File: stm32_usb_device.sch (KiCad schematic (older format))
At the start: 43 parts, among them J1 USB_A, J2 Conn_01x05, J3 Conn_01x03, SW1 RST_SW, SW2 USR_SW, U1 HT7533-1, U2 SRV05-4, U3 STM32F103C8T6, Y1 16M

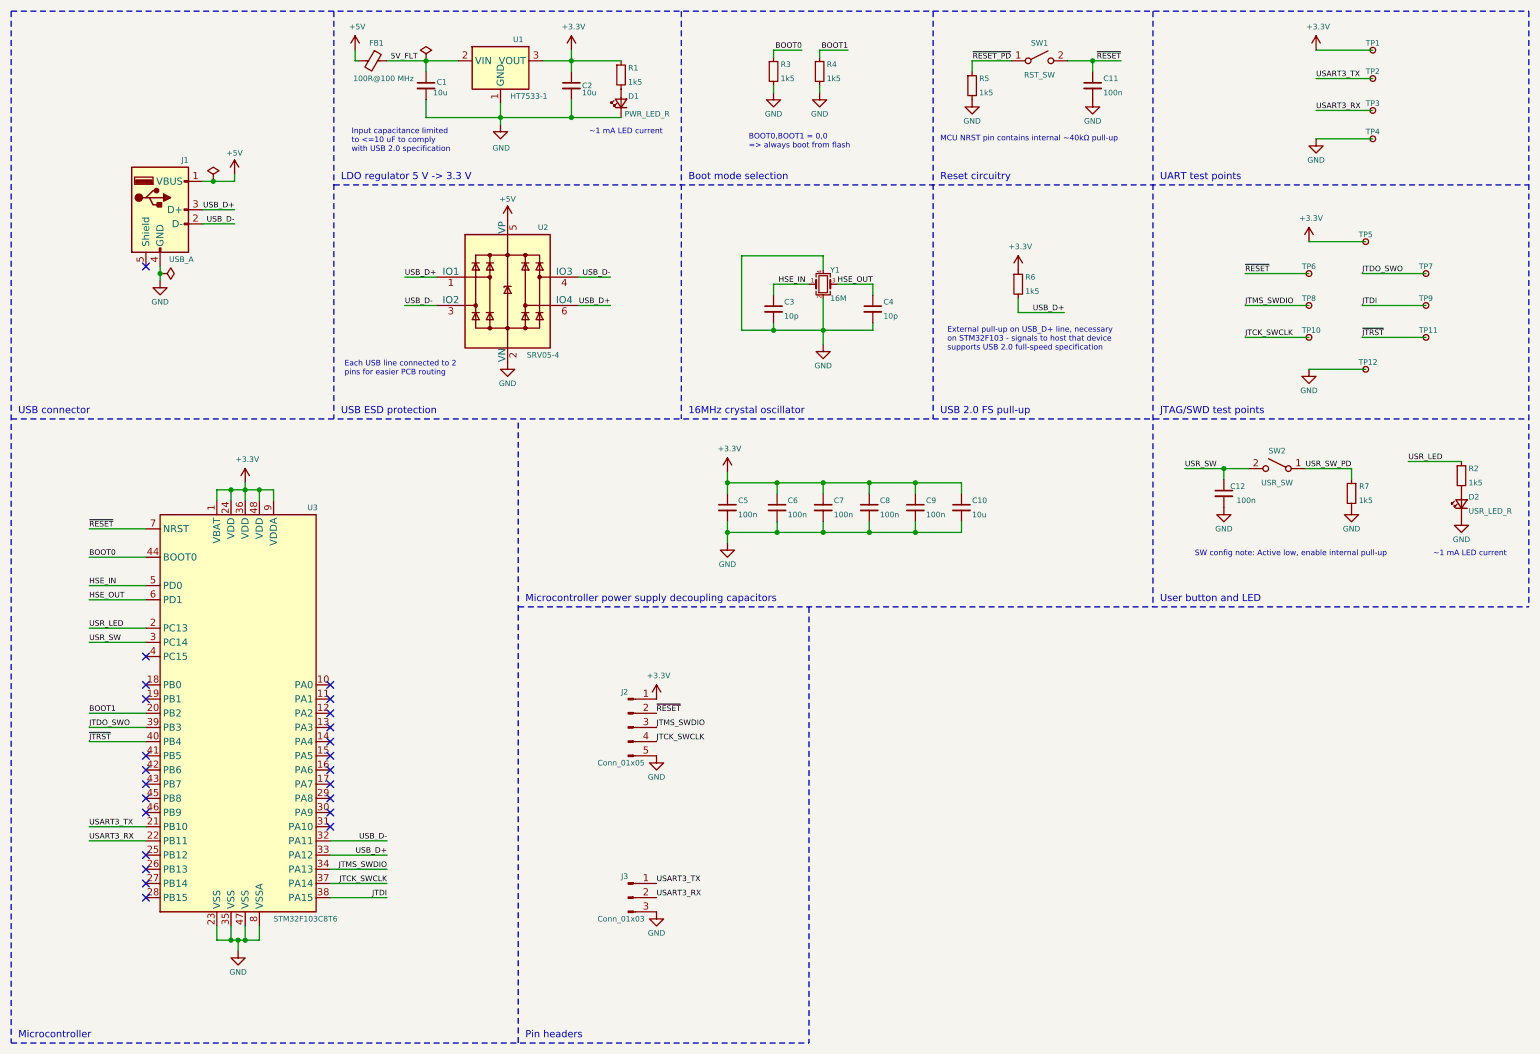
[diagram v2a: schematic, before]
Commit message: Add USB connector and UART isolators
Make initial PCB layout and routing
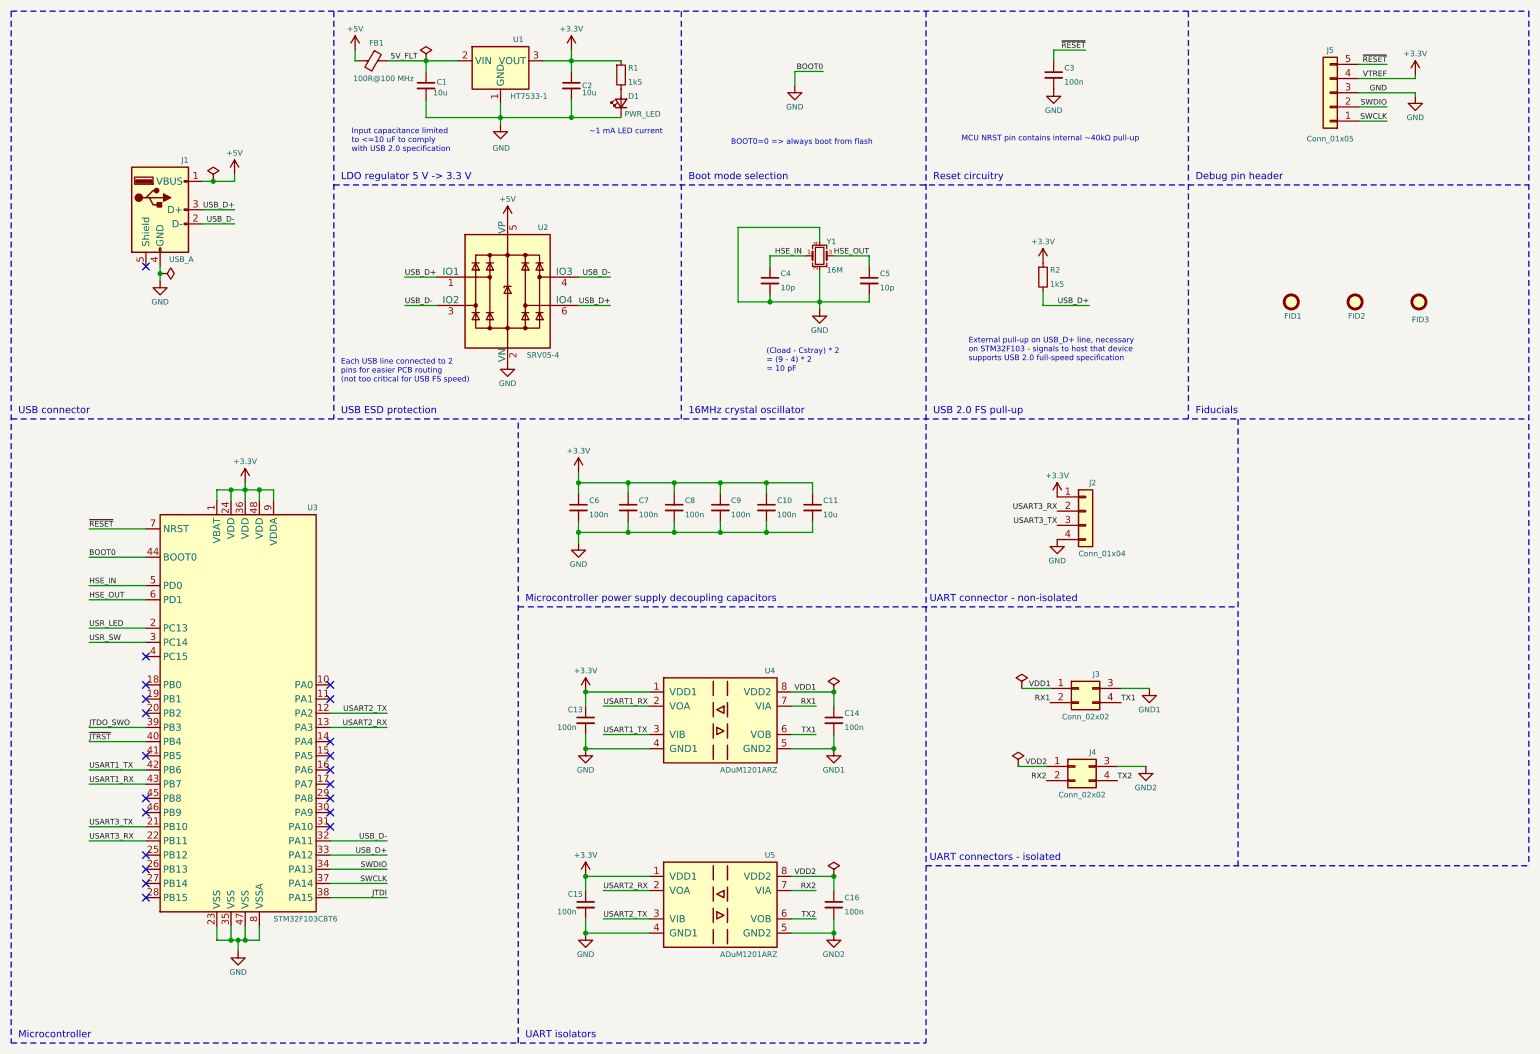
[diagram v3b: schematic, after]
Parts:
- removed C12: 100n, Capacitor_SMD:C_0402_1005Metric, symbol Device:C_Small
- removed D2: USR_LED_R, LED_SMD:LED_0603_1608Metric, symbol Device:LED_Small
- removed J2: Conn_01x05, Connector_PinHeader_2.54mm:PinHeader_1x05_P2.54mm_Vertical, symbol Connector:Conn_01x05_Male
- removed J3: Conn_01x03, Connector_PinHeader_2.54mm:PinHeader_1x03_P2.54mm_Vertical, symbol Connector:Conn_01x03_Male
- removed R2, R3, R4, R5, R7: 1k5, Resistor_SMD:R_0402_1005Metric, symbol Device:R_Small
- removed SW1: RST_SW, Button_Switch_SMD:SW_SPST_CK_RS282G05A3, symbol Switch:SW_SPST
- removed SW2: USR_SW, Button_Switch_SMD:SW_SPST_CK_RS282G05A3, symbol Switch:SW_SPST
- removed TP1, TP10, TP11, TP12, TP2, TP3, TP4, TP5, TP6, TP7, TP8, TP9: TestPoint_Small, TestPoint:TestPoint_Pad_D1.0mm, symbol Connector:TestPoint_Small
- added C13, C14, C15, C16: 100n, Capacitor_SMD:C_0402_1005Metric, symbol Device:C_Small
- added FID1, FID2, FID3: Fiducial, Fiducial:Fiducial_1mm_Mask2mm, symbol Mechanical:Fiducial
- added J2: Conn_01x04, Connector_PinHeader_2.54mm:PinHeader_1x04_P2.54mm_Vertical, symbol Connector_Generic:Conn_01x04
- added J3, J4: Conn_02x02, Connector_PinHeader_2.54mm:PinHeader_2x02_P2.54mm_Horizontal, symbol Connector_Generic:Conn_02x02_Top_Bottom
- added J5: Conn_01x05, Connector_PinHeader_1.27mm:PinHeader_1x05_P1.27mm_Vertical_SMD_Pin1Left, symbol Connector_Generic:Conn_01x05
- added U4, U5: ADuM1201ARZ, Package_SO:SOIC-8_3.9x4.9mm_P1.27mm, symbol Isolator:ADuM1201AR
- D1: value PWR_LED_R -> PWR_LED
- J1: footprint Connector_USB:USB_A_CNCTech_1001-011-01101_Horizontal -> USB_A_connector:USB_A_4pin
- renumbered C9 to C10, C10 to C11, C11 to C3, C3 to C4, C4 to C5, C5 to C6, C6 to C7, C7 to C8, C8 to C9, R6 to R2
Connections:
- net BOOT0 is gone; now on net GND: U3.44 (BOOT0)
- net +3V3: now also C13.1, C15.1, J2.1 (Pin_1), J5.4 (Pin_4), U4.1 (VDD1), U5.1 (VDD1)
- net GND: now also C13.2, C15.2, J2.4 (Pin_4), J5.3 (Pin_3), U4.4 (GND1), U5.4 (GND1)
- net USART3_RX: now also J2.2 (Pin_2)
- net USART3_TX: now also J2.3 (Pin_3)
- net ~RESET: now also J5.5 (Pin_5)
- net USART2_TX: now reaches U3.12 (PA2)
- net USART2_TX: now also U5.3 (VIB)
- net USART2_RX: now reaches U3.13 (PA3)
- net USART2_RX: now also U5.2 (VOA)
- net USART1_TX: now reaches U3.42 (PB6)
- net USART1_TX: now also U4.3 (VIB)
- net USART1_RX: now reaches U3.43 (PB7)
- net USART1_RX: now also U4.2 (VOA)
- net BOOT1: no longer names the net of U3.20 (PB2)
- net JTCK_SWCLK renamed SWCLK
- net SWCLK: now also J5.1 (Pin_1)
- net JTMS_SWDIO renamed SWDIO
- net SWDIO: now also J5.2 (Pin_2)
- new net GND1: C14.2, J3.3 (Pin_3), U4.5 (GND2)
- new net GND2: C16.2, J4.3 (Pin_3), U5.5 (GND2)
- new net RX1: J3.2 (Pin_2), U4.7 (VIA)
- new net RX2: J4.2 (Pin_2), U5.7 (VIA)
- new net TX1: J3.4 (Pin_4), U4.6 (VOB)
- new net TX2: J4.4 (Pin_4), U5.6 (VOB)
- new net VDD1: C14.1, J3.1 (Pin_1), U4.8 (VDD2)
- new net VDD2: C16.1, J4.1 (Pin_1), U5.8 (VDD2)
- no-connect marks 24 -> 21
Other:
- note added: "(Cload - Cstray) * 2\n= (9 - 4) * 2\n= 10 pF"
- note added: "BOOT0=0 => always boot from flash"
- note added: "Debug pin header"
- note added: "Each USB line connected to 2\npins for easier PCB routing\n(not too critical for USB FS speed)"
- note added: "Fiducials"
- note added: "UART connector - non-isolated"
- note added: "UART connectors - isolated"
- note added: "UART isolators"
- note removed: "BOOT0,BOOT1 = 0,0\n=> always boot from flash"
- note removed: "Each USB line connected to 2\npins for easier PCB routing"
- note removed: "JTAG/SWD test points"
- note removed: "Pin headers"
- note removed: "SW config note: Active low, enable internal pull-up"
- note removed: "UART test points"
- note removed: "User button and LED"
- moved on the sheet: C10, C11, C3, C4, C5, C6, C7, C8, C9, R2, Y1

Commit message: Finish PCB routing
Signed-off-by: Tomislav Milkovic <tomislav.milkovic95@gmail.com>
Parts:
- removed C13, C14, C15, C16: 100n, Capacitor_SMD:C_0402_1005Metric, symbol Device:C_Small
- removed J3, J4: Conn_02x02, Connector_PinHeader_2.54mm:PinHeader_2x02_P2.54mm_Horizontal, symbol Connector_Generic:Conn_02x02_Top_Bottom
- removed U4, U5: ADuM1201ARZ, Package_SO:SOIC-8_3.9x4.9mm_P1.27mm, symbol Isolator:ADuM1201AR
- added J1, J2: Conn_01x04, Connector_PinHeader_2.54mm:PinHeader_1x04_P2.54mm_Vertical, symbol Connector_Generic:Conn_01x04
- added R3, R4, R5, R6, R7, R8: 510R, Resistor_SMD:R_0402_1005Metric, symbol Device:R_Small
- C1, C11, C2: JLCPCB Part # (none) -> C96446
- C10, C3, C6, C7, C8, C9: JLCPCB Part # (none) -> C307331
- C4, C5: JLCPCB Part # (none) -> C32949
- FB1: JLCPCB Part # (none) -> C1015
- R1, R2: JLCPCB Part # (none) -> C25867
- U1: JLCPCB Part # (none) -> C14289
- U2: JLCPCB Part # (none) -> C7420376
- U3: JLCPCB Part # (none) -> C8734
- Y1: JLCPCB Part # (none) -> C13738
- renumbered J2 to J3, J1 to J4
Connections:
- net +3V3: now also J1.1 (Pin_1), J2.1 (Pin_1)
- net GND: now also J1.4 (Pin_4), J2.4 (Pin_4)
- net USART1_RX: now also R7.1
- net USART1_TX: now also R8.2
- net USART2_RX: now also R3.1
- net USART2_TX: now also R4.2
- net USART3_RX: now also R5.1; no longer J3.2 (Pin_2)
- net USART3_TX: now also R6.2; no longer J3.3 (Pin_3)
- new net: J1.2 (Pin_2), R7.2
- new net: J1.3 (Pin_3), R8.1
- new net: J2.2 (Pin_2), R3.2
- new net: J2.3 (Pin_3), R4.1
- new net: J3.2 (Pin_2), R5.2
- new net: J3.3 (Pin_3), R6.1
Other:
- note added: "MCU power supply decoupling capacitors"
- note added: "UART connectors"
- note removed: "Microcontroller power supply decoupling capacitors"
- note removed: "UART connector - non-isolated"
- note removed: "UART connectors - isolated"
- note removed: "UART isolators"
- moved on the sheet: J3

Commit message: Remove unused net labels
Signed-off-by: Tomislav Milkovic <tomislav.milkovic95@gmail.com>
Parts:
- C1, C11, C2: JLCPCB Part # C96446 -> (none); LCSC (none) -> C96446
- C10, C3, C6, C7, C8, C9: JLCPCB Part # C307331 -> (none); LCSC (none) -> C307331
- C4, C5: JLCPCB Part # C32949 -> (none); LCSC (none) -> C32949
- D1: LCSC (none) -> C2286
- FB1: JLCPCB Part # C1015 -> (none); LCSC (none) -> C1015
- R1, R2: JLCPCB Part # C25867 -> (none); LCSC (none) -> C25867
- R3, R4, R5, R6, R7, R8: JLCPCB Part # C25123 -> (none); LCSC (none) -> C25123
- U1: JLCPCB Part # C14289 -> (none); LCSC (none) -> C14289
- U2: JLCPCB Part # C7420376 -> (none); LCSC (none) -> C7420376
- U3: JLCPCB Part # C8734 -> (none); LCSC (none) -> C8734
- Y1: JLCPCB Part # C13738 -> (none); LCSC (none) -> C13738
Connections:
- net JTDI: no longer names the net of U3.38 (PA15)
- net JTDO_SWO: no longer names the net of U3.39 (PB3)
- net USR_LED: no longer names the net of U3.2 (PC13)
- net USR_SW: no longer names the net of U3.3 (PC14)
- net ~JTRST: no longer names the net of U3.40 (PB4)
- no-connect marks 21 -> 26
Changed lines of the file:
@@
 F 2 "Package_QFP:LQFP-48_7x7mm_P0.5mm" H 1550 4050 50  0001 R CNN
 F 3 "http://www.st.com/st-web-ui/static/active/en/resource/technical/document/datasheet/CD00161566.pdf" H 2150 5450 50  0001 C CNN
-F 4 "C8734" H 2150 5450 50  0001 C CNN "JLCPCB Part #"
+F 4 "C8734" H 2150 5450 50  0001 C CNN "LCSC"
 	1    2150 5450
 	1    0    0    -1
@@
 F 2 "Package_TO_SOT_SMD:SOT-89-3" H 3950 1275 50  0001 C CIN
 F 3 "https://www.holtek.com/documents/10179/116711/HT75xx-1v250.pdf" H 3950 1050 50  0001 C CNN
-F 4 "C14289" H 3950 950 50  0001 C CNN "JLCPCB Part #"
+F 4 "C14289" H 3950 950 50  0001 C CNN "LCSC"
 	1    3950 950
 	1    0    0    -1
@@
 F 2 "Package_TO_SOT_SMD:SOT-23-6" H 4700 2025 50  0001 C CNN
 F 3 "http://www.onsemi.com/pub/Collateral/SRV05-4-D.PDF" H 4000 2475 50  0001 C CNN
-F 4 "C7420376" H 4000 2475 50  0001 C CNN "JLCPCB Part #"
+F 4 "C7420376" H 4000 2475 50  0001 C CNN "LCSC"
 	1    4000 2475
 	1    0    0    -1
@@
 F 2 "Capacitor_SMD:C_0603_1608Metric" H 3425 1025 50  0001 C CNN
 F 3 "~" H 3425 1025 50  0001 C CNN
-F 4 "C96446" H 3425 1025 50  0001 C CNN "JLCPCB Part #"
+F 4 "C96446" H 3425 1025 50  0001 C CNN "LCSC"
 	1    3425 1025
 	1    0    0    -1
@@
 F 2 "Capacitor_SMD:C_0603_1608Metric" H 4450 1025 50  0001 C CNN
 F 3 "~" H 4450 1025 50  0001 C CNN
-F 4 "C96446" H 4450 1025 50  0001 C CNN "JLCPCB Part #"
+F 4 "C96446" H 4450 1025 50  0001 C CNN "LCSC"
 	1    4450 1025
 	1    0    0    -1
@@
 F 2 "Capacitor_SMD:C_0402_1005Metric" H 7850 950 50  0001 C CNN
 F 3 "~" H 7850 950 50  0001 C CNN
-F 4 "C307331" H 7850 950 50  0001 C CNN "JLCPCB Part #"
+F 4 "C307331" H 7850 950 50  0001 C CNN "LCSC"
 	1    7850 950
 	1    0    0    -1
@@
 F 2 "Crystal:Crystal_SMD_3225-4Pin_3.2x2.5mm" H 6200 2225 50  0001 C CNN
 F 3 "~" H 6200 2225 50  0001 C CNN
-F 4 "C13738" H 6200 2225 50  0001 C CNN "JLCPCB Part #"
+F 4 "C13738" H 6200 2225 50  0001 C CNN "LCSC"
 	1    6200 2225
 	1    0    0    -1
@@
 F 2 "Capacitor_SMD:C_0402_1005Metric" H 6550 2400 50  0001 C CNN
 F 3 "~" H 6550 2400 50  0001 C CNN
-F 4 "C32949" H 6550 2400 50  0001 C CNN "JLCPCB Part #"
+F 4 "C32949" H 6550 2400 50  0001 C CNN "LCSC"
 	1    6550 2400
 	1    0    0    -1
@@
 F 2 "Capacitor_SMD:C_0402_1005Metric" H 5850 2400 50  0001 C CNN
 F 3 "~" H 5850 2400 50  0001 C CNN
-F 4 "C32949" H 5850 2400 50  0001 C CNN "JLCPCB Part #"
+F 4 "C32949" H 5850 2400 50  0001 C CNN "LCSC"
 	1    5850 2400
 	1    0    0    -1
@@
 F 2 "Resistor_SMD:R_0402_1005Metric" H 7775 2375 50  0001 C CNN
 F 3 "~" H 7775 2375 50  0001 C CNN
-F 4 "C25867" H 7775 2375 50  0001 C CNN "JLCPCB Part #"
+F 4 "C25867" H 7775 2375 50  0001 C CNN "LCSC"
 	1    7775 2375
 	1    0    0    -1
@@
 Text Label 1050 6350 0    39   ~ 0
 USART3_RX
-Text Label 3150 6750 2    39   ~ 0
-JTDI
-Text Label 1050 5550 0    39   ~ 0
-JTDO_SWO
-Text Label 1050 5650 0    39   ~ 0
-~JTRST
 Wire Wire Line
 	2750 6650 3150 6650
@@
 Wire Wire Line
 	2750 6350 3150 6350
-Wire Wire Line
-	2750 6750 3150 6750
-Wire Wire Line
-	1450 5550 1050 5550
-Wire Wire Line
-	1050 5650 1450 5650
 Wire Wire Line
 	1050 6350 1450 6350
@@
 F 2 "Resistor_SMD:R_0402_1005Metric" H 4800 950 50  0001 C CNN
 F 3 "~" H 4800 950 50  0001 C CNN
-F 4 "C25867" H 4800 950 50  0001 C CNN "JLCPCB Part #"
+F 4 "C25867" H 4800 950 50  0001 C CNN "LCSC"
 	1    4800 950
 	1    0    0    -1
@@
 F 2 "LED_SMD:LED_0603_1608Metric" V 4800 1150 50  0001 C CNN
 F 3 "~" V 4800 1150 50  0001 C CNN
-F 4 "" V 4800 1150 50  0001 C CNN "JLCPCB Part #"
+F 4 "C2286" V 4800 1150 50  0001 C CNN "LCSC"
 	1    4800 1150
 	0    -1   -1   0
@@
 F 2 "Capacitor_SMD:C_0402_1005Metric" H 5175 4000 50  0001 C CNN
 F 3 "~" H 5175 4000 50  0001 C CNN
-F 4 "C307331" H 5175 4000 50  0001 C CNN "JLCPCB Part #"
+F 4 "C307331" H 5175 4000 50  0001 C CNN "LCSC"
 	1    5175 4000
 	1    0    0    -1
@@
 F 2 "Capacitor_SMD:C_0402_1005Metric" H 5500 4000 50  0001 C CNN
 F 3 "~" H 5500 4000 50  0001 C CNN
-F 4 "C307331" H 5500 4000 50  0001 C CNN "JLCPCB Part #"
+F 4 "C307331" H 5500 4000 50  0001 C CNN "LCSC"
 	1    5500 4000
 	1    0    0    -1
@@
 F 2 "Capacitor_SMD:C_0402_1005Metric" H 5825 4000 50  0001 C CNN
 F 3 "~" H 5825 4000 50  0001 C CNN
-F 4 "C307331" H 5825 4000 50  0001 C CNN "JLCPCB Part #"
+F 4 "C307331" H 5825 4000 50  0001 C CNN "LCSC"
 	1    5825 4000
 	1    0    0    -1
@@
 F 2 "Capacitor_SMD:C_0402_1005Metric" H 4500 4000 50  0001 C CNN
 F 3 "~" H 4500 4000 50  0001 C CNN
-F 4 "C307331" H 4500 4000 50  0001 C CNN "JLCPCB Part #"
+F 4 "C307331" H 4500 4000 50  0001 C CNN "LCSC"
 	1    4500 4000
 	1    0    0    -1
 $EndComp
-Wire Wire Line
-	1450 4850 1050 4850
-Text Label 1050 4850 0    39   ~ 0
-USR_LED
 $Comp
 L power:+3.3V #PWR018
@@
 Text Notes 4575 1375 0    39   ~ 0
 ~~1 mA LED current
-Wire Wire Line
-	1450 4950 1050 4950
-Text Label 1050 4950 0    39   ~ 0
-USR_SW
 Wire Notes Line
 	4075 7775 4075 3375
@@
 F 2 "Inductor_SMD:L_0805_2012Metric" V 2980 850 50  0001 C CNN
 F 3 "~" H 3050 850 50  0001 C CNN
-F 4 "C1015" V 3050 850 50  0001 C CNN "JLCPCB Part #"
+F 4 "C1015" V 3050 850 50  0001 C CNN "LCSC"
 	1    3050 850
 	0    1    1    0
@@
 F 2 "USB_A_connector:USB_A_4pin" H 1700 1850 50  0001 C CNN
 F 3 " ~" H 1700 1850 50  0001 C CNN
-F 4 "" H 1550 1900 50  0001 C CNN "JLCPCB Part #"
+F 4 "" H 1550 1900 50  0001 C CNN "LCSC"
 	1    1550 1900
 	1    0    0    -1
@@
 F 2 "Capacitor_SMD:C_0402_1005Metric" H 4850 4000 50  0001 C CNN
 F 3 "~" H 4850 4000 50  0001 C CNN
-F 4 "C307331" H 4850 4000 50  0001 C CNN "JLCPCB Part #"
+F 4 "C307331" H 4850 4000 50  0001 C CNN "LCSC"
 	1    4850 4000
 	1    0    0    -1
@@
 F 2 "Capacitor_SMD:C_0603_1608Metric" H 6150 4000 50  0001 C CNN
 F 3 "~" H 6150 4000 50  0001 C CNN
-F 4 "C96446" H 6150 4000 50  0001 C CNN "JLCPCB Part #"
+F 4 "C96446" H 6150 4000 50  0001 C CNN "LCSC"
 	1    6150 4000
 	1    0    0    -1
@@
 F 2 "Connector_PinHeader_1.27mm:PinHeader_1x05_P1.27mm_Vertical_SMD_Pin1Left" H 9800 1075 50  0001 C CNN
 F 3 "~" H 9800 1075 50  0001 C CNN
-F 4 "" H 9800 1075 50  0001 C CNN "JLCPCB Part #"
+F 4 "" H 9800 1075 50  0001 C CNN "LCSC"
 	1    9800 1075
 	-1   0    0    1
@@
 F 2 "Resistor_SMD:R_0402_1005Metric" H 5250 5300 50  0001 C CNN
 F 3 "~" H 5250 5300 50  0001 C CNN
-F 4 "C25123" V 5250 5300 50  0001 C CNN "JLCPCB Part #"
+F 4 "C25123" V 5250 5300 50  0001 C CNN "LCSC"
 	1    5250 5300
 	0    -1   -1   0
@@
 F 2 "Resistor_SMD:R_0402_1005Metric" H 5250 5400 50  0001 C CNN
 F 3 "~" H 5250 5400 50  0001 C CNN
-F 4 "C25123" V 5250 5400 50  0001 C CNN "JLCPCB Part #"
+F 4 "C25123" V 5250 5400 50  0001 C CNN "LCSC"
 	1    5250 5400
 	0    1    1    0
@@
 F 2 "Resistor_SMD:R_0402_1005Metric" H 5250 7000 50  0001 C CNN
 F 3 "~" H 5250 7000 50  0001 C CNN
-F 4 "C25123" V 5250 7000 50  0001 C CNN "JLCPCB Part #"
+F 4 "C25123" V 5250 7000 50  0001 C CNN "LCSC"
 	1    5250 7000
 	0    -1   -1   0
@@
 F 2 "Resistor_SMD:R_0402_1005Metric" H 5250 7100 50  0001 C CNN
 F 3 "~" H 5250 7100 50  0001 C CNN
-F 4 "C25123" V 5250 7100 50  0001 C CNN "JLCPCB Part #"
+F 4 "C25123" V 5250 7100 50  0001 C CNN "LCSC"
 	1    5250 7100
 	0    1    1    0
@@
 F 2 "Resistor_SMD:R_0402_1005Metric" H 5250 6250 50  0001 C CNN
 F 3 "~" H 5250 6250 50  0001 C CNN
-F 4 "C25123" V 5250 6250 50  0001 C CNN "JLCPCB Part #"
+F 4 "C25123" V 5250 6250 50  0001 C CNN "LCSC"
 	1    5250 6250
 	0    1    1    0
@@
 F 2 "Resistor_SMD:R_0402_1005Metric" H 5250 6150 50  0001 C CNN
 F 3 "~" H 5250 6150 50  0001 C CNN
-F 4 "C25123" V 5250 6150 50  0001 C CNN "JLCPCB Part #"
+F 4 "C25123" V 5250 6150 50  0001 C CNN "LCSC"
 	1    5250 6150
 	0    -1   -1   0
 $EndComp
+NoConn ~ 1450 4850
+NoConn ~ 1450 4950
+NoConn ~ 2750 6750
+NoConn ~ 1450 5550
+NoConn ~ 1450 5650
 $EndSCHEMATC
